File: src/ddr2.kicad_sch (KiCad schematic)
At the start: 7 parts, among them U2 IS43DR86400E

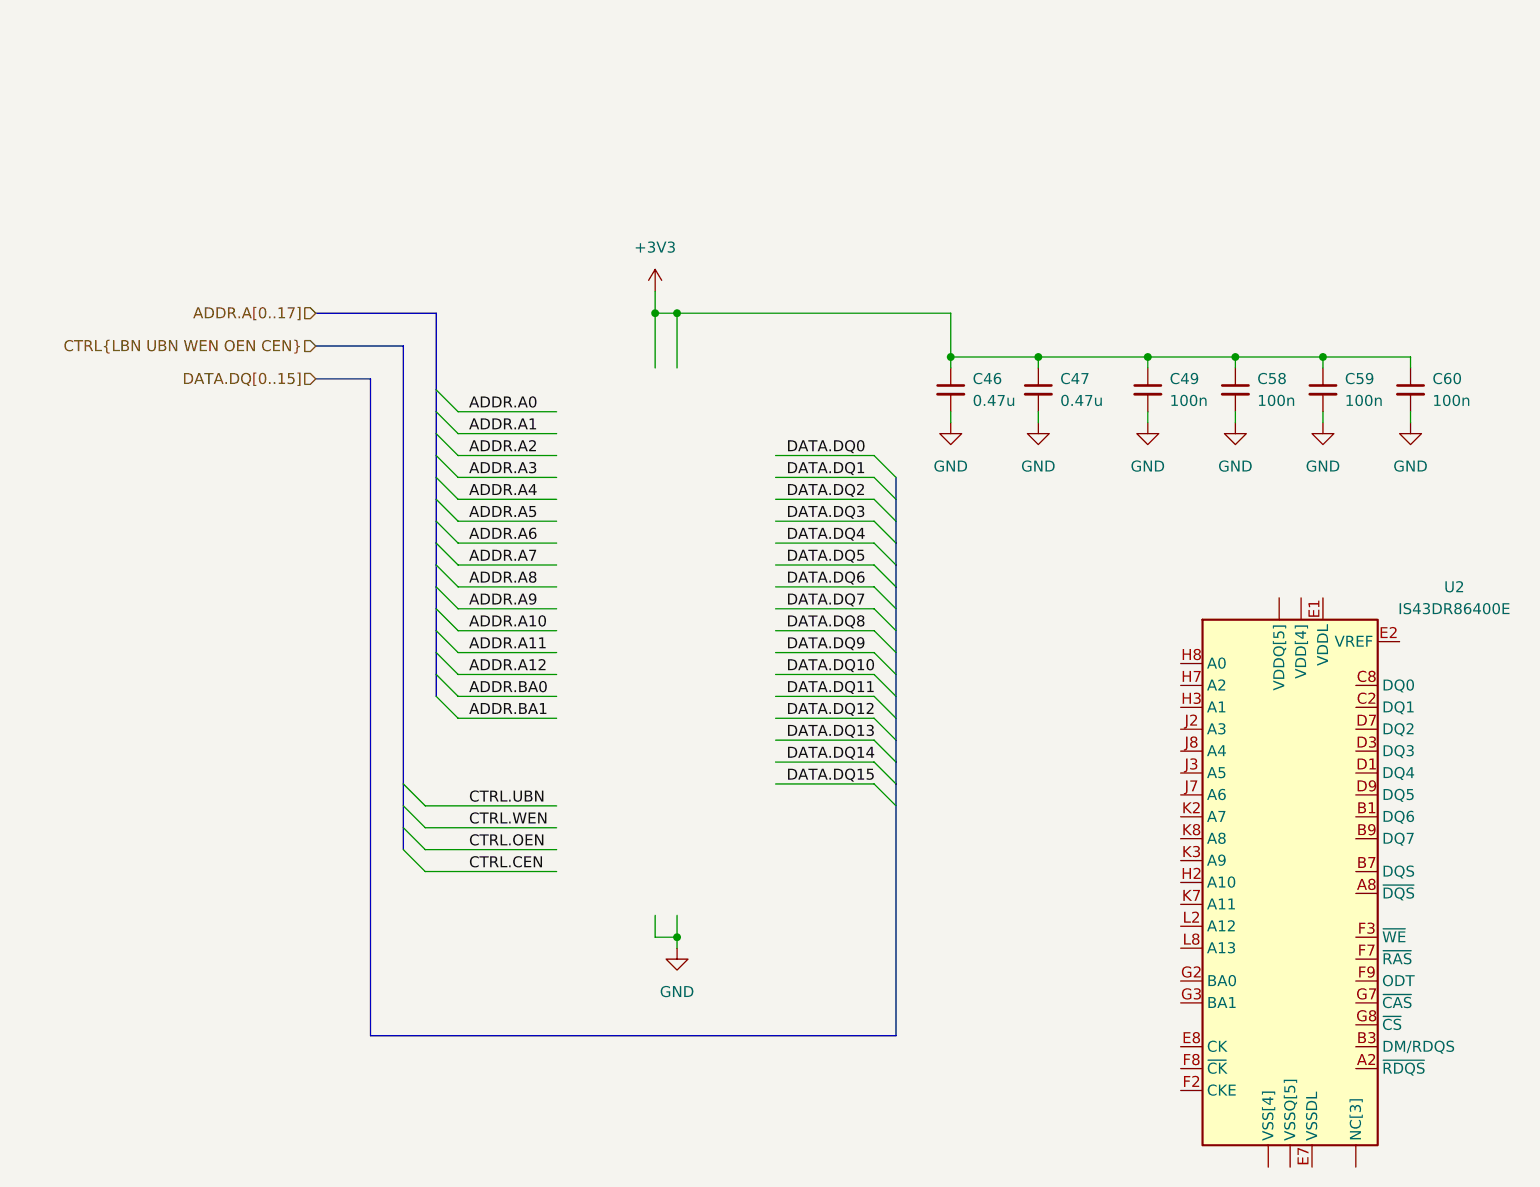
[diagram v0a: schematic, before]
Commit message: Adds DDR2 schematic
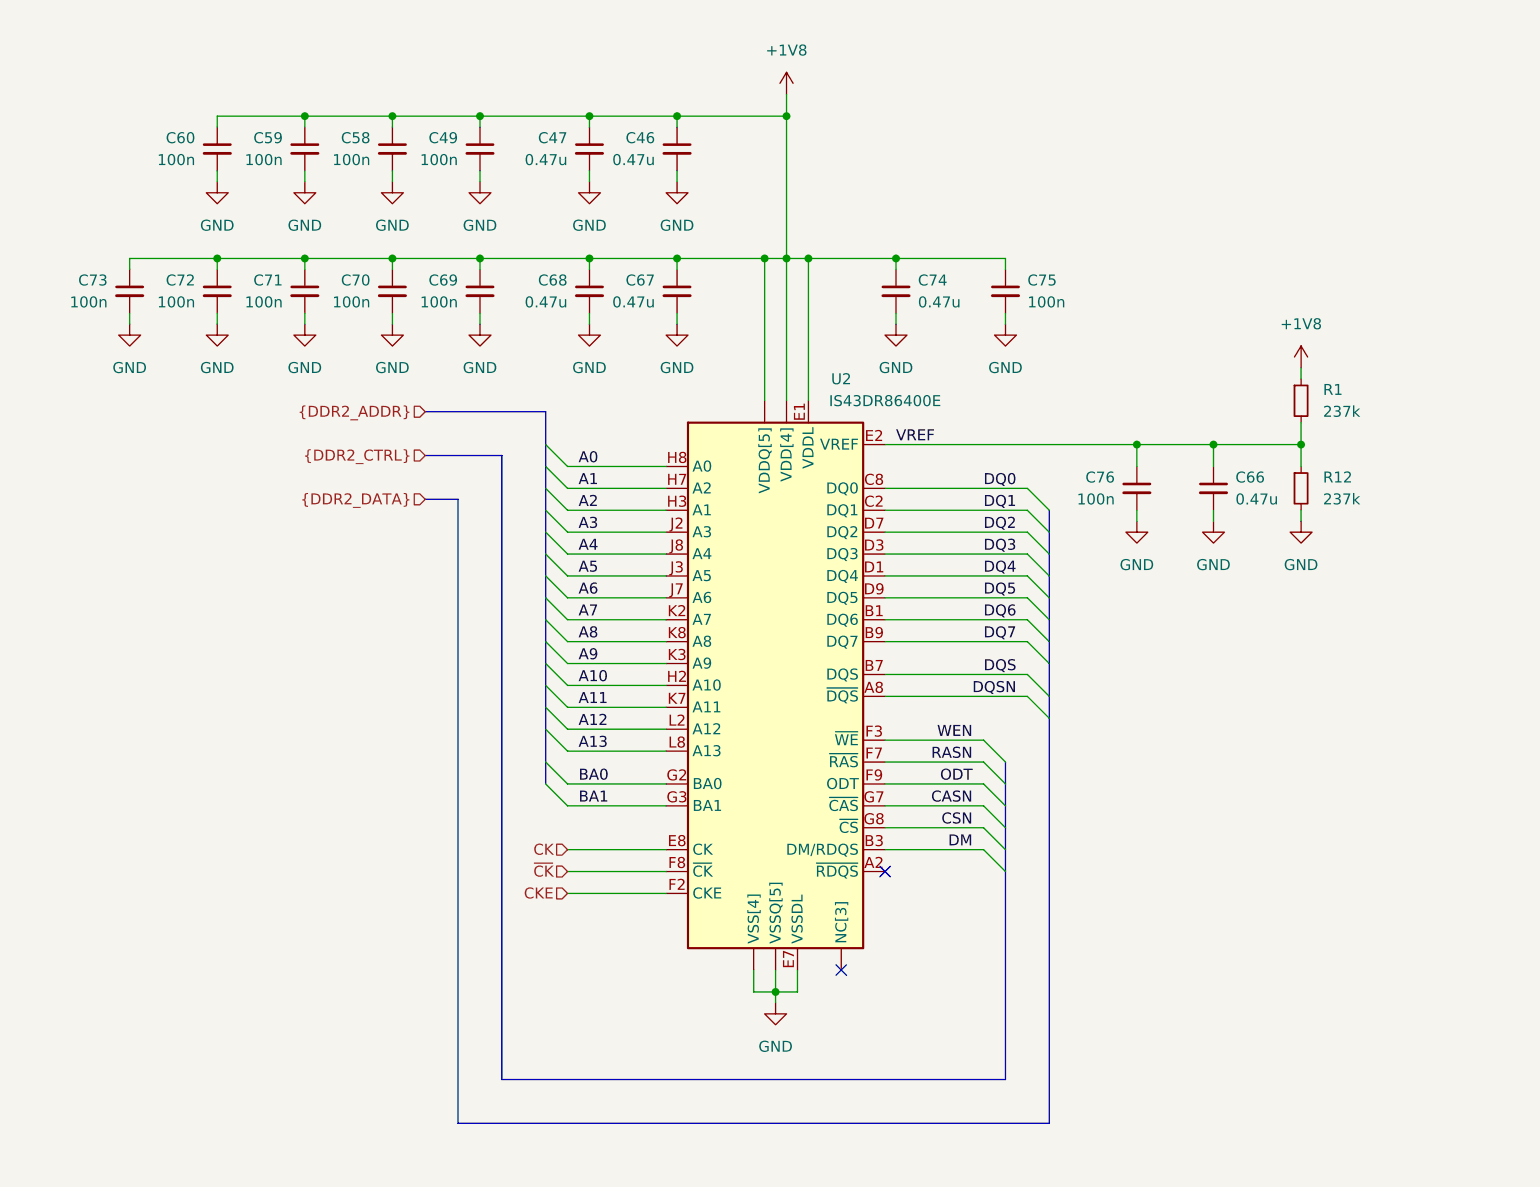
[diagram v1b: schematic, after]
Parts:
- added C66, C67, C68, C74: 0.47u, symbol Device:C_Small
- added C69, C70, C71, C72, C73, C75, C76: 100n, symbol Device:C_Small
- added R1, R12: 237k, symbol Device:R_Small
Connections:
- net +3V3 is gone; now on net +1V8: C46.1, C47.1, C49.1, C58.1, C59.1, C60.1
- net GND: now also U2. (VSS[4]), U2.A3 (VSS), U2.A7 (VSSQ), U2.B2 (VSSQ), U2.B8 (VSSQ), U2.D2 (VSSQ), U2.D8 (VSSQ), U2.E3 (VSS), U2.E7 (VSSDL), U2.J1 (VSS), U2.K9 (VSS), C66.2, C67.2, C68.2, C69.2, C70.2, C71.2, C72.2, C73.2, C74.2, C75.2, C76.2, R12.2
- net +1V8: now reaches U2. (VSS[4]), U2.A1 (VDD), U2.E9 (VDD), U2.H9 (VDD), U2.L1 (VDD)
- net +1V8: now also U2.A9 (VDDQ), U2.C1 (VDDQ), U2.C3 (VDDQ), U2.C7 (VDDQ), U2.C9 (VDDQ), U2.E1 (VDDL), C67.1, C68.1, C69.1, C70.1, C71.1, C72.1, C73.1, C74.1, C75.1, R1.1
- net DQSN: now reaches U2.A8 (~{DQS})
- net DQ6: now reaches U2.B1 (DQ6)
- net DM: now reaches U2.B3 (DM/RDQS)
- net DQS: now reaches U2.B7 (DQS)
- net DQ7: now reaches U2.B9 (DQ7)
- net DQ1: now reaches U2.C2 (DQ1)
- net DQ0: now reaches U2.C8 (DQ0)
- net DQ4: now reaches U2.D1 (DQ4)
- net DQ3: now reaches U2.D3 (DQ3)
- net DQ2: now reaches U2.D7 (DQ2)
- net DQ5: now reaches U2.D9 (DQ5)
- net VREF: now reaches U2.E2 (VREF)
- net VREF: now also C66.1, C76.1, R1.2, R12.1
- net CK: now reaches U2.E8 (CK)
- net CKE: now reaches U2.F2 (CKE)
- net WEN: now reaches U2.F3 (~{WE})
- net RASN: now reaches U2.F7 (~{RAS})
- net ~{CK}: now reaches U2.F8 (~{CK})
- net ODT: now reaches U2.F9 (ODT)
- net BA0: now reaches U2.G2 (BA0)
- net BA1: now reaches U2.G3 (BA1)
- net CASN: now reaches U2.G7 (~{CAS})
- net CSN: now reaches U2.G8 (~{CS})
- net A10: now reaches U2.H2 (A10)
- net A2: now reaches U2.H3 (A1)
- net A1: now reaches U2.H7 (A2)
- net A0: now reaches U2.H8 (A0)
- net A3: now reaches U2.J2 (A3)
- net A5: now reaches U2.J3 (A5)
- net A6: now reaches U2.J7 (A6)
- net A4: now reaches U2.J8 (A4)
- net A7: now reaches U2.K2 (A7)
- net A9: now reaches U2.K3 (A9)
- net A11: now reaches U2.K7 (A11)
- net A8: now reaches U2.K8 (A8)
- net A12: now reaches U2.L2 (A12)
- net A13: now reaches U2.L8 (A13)
- no-connect marks 0 -> 2
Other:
- moved on the sheet: U2

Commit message: Finishes the ram schematic
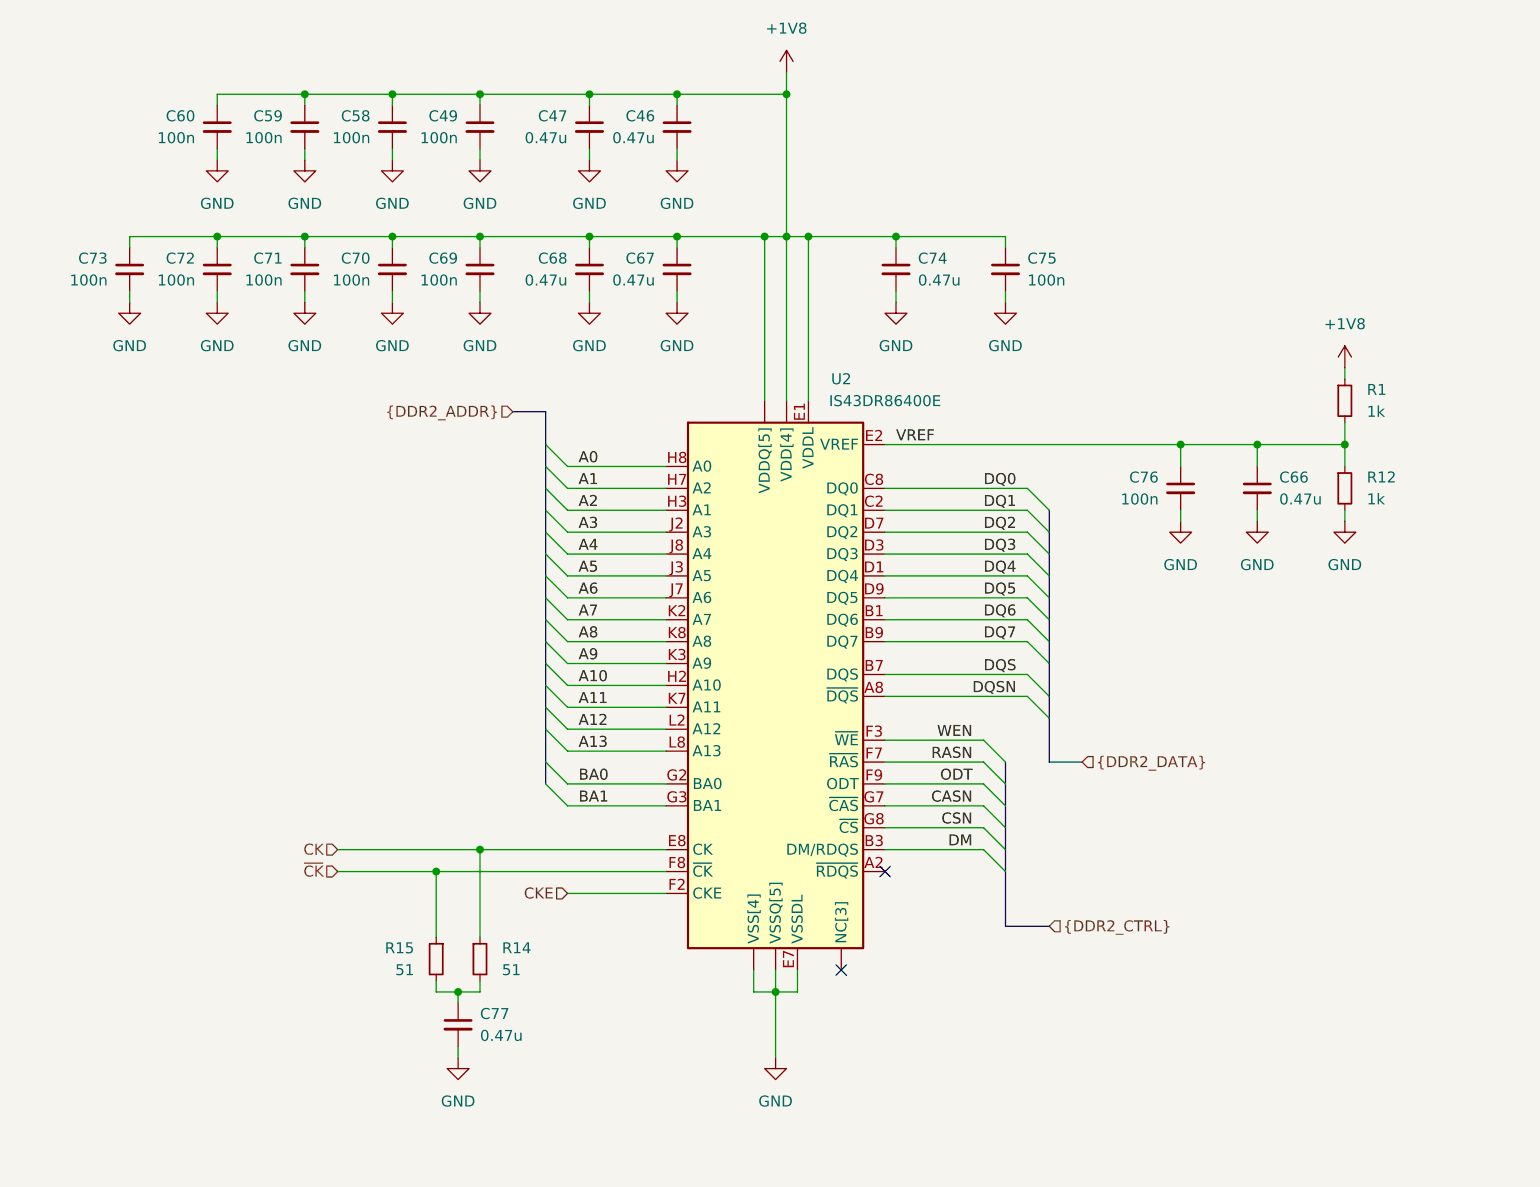
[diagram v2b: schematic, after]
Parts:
- added C77: 0.47u, symbol Device:C_Small
- added R14, R15: 51, symbol Device:R_Small
- R1, R12: value 237k -> 1k
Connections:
- net CK: now also R14.1
- net GND: now also C77.2
- net ~{CK}: now also R15.1
- new net: C77.1, R14.2, R15.2
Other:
- moved on the sheet: C46, C47, C49, C58, C59, C60, C66, C67, C68, C69, C70, C71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

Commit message: Add the eMMC
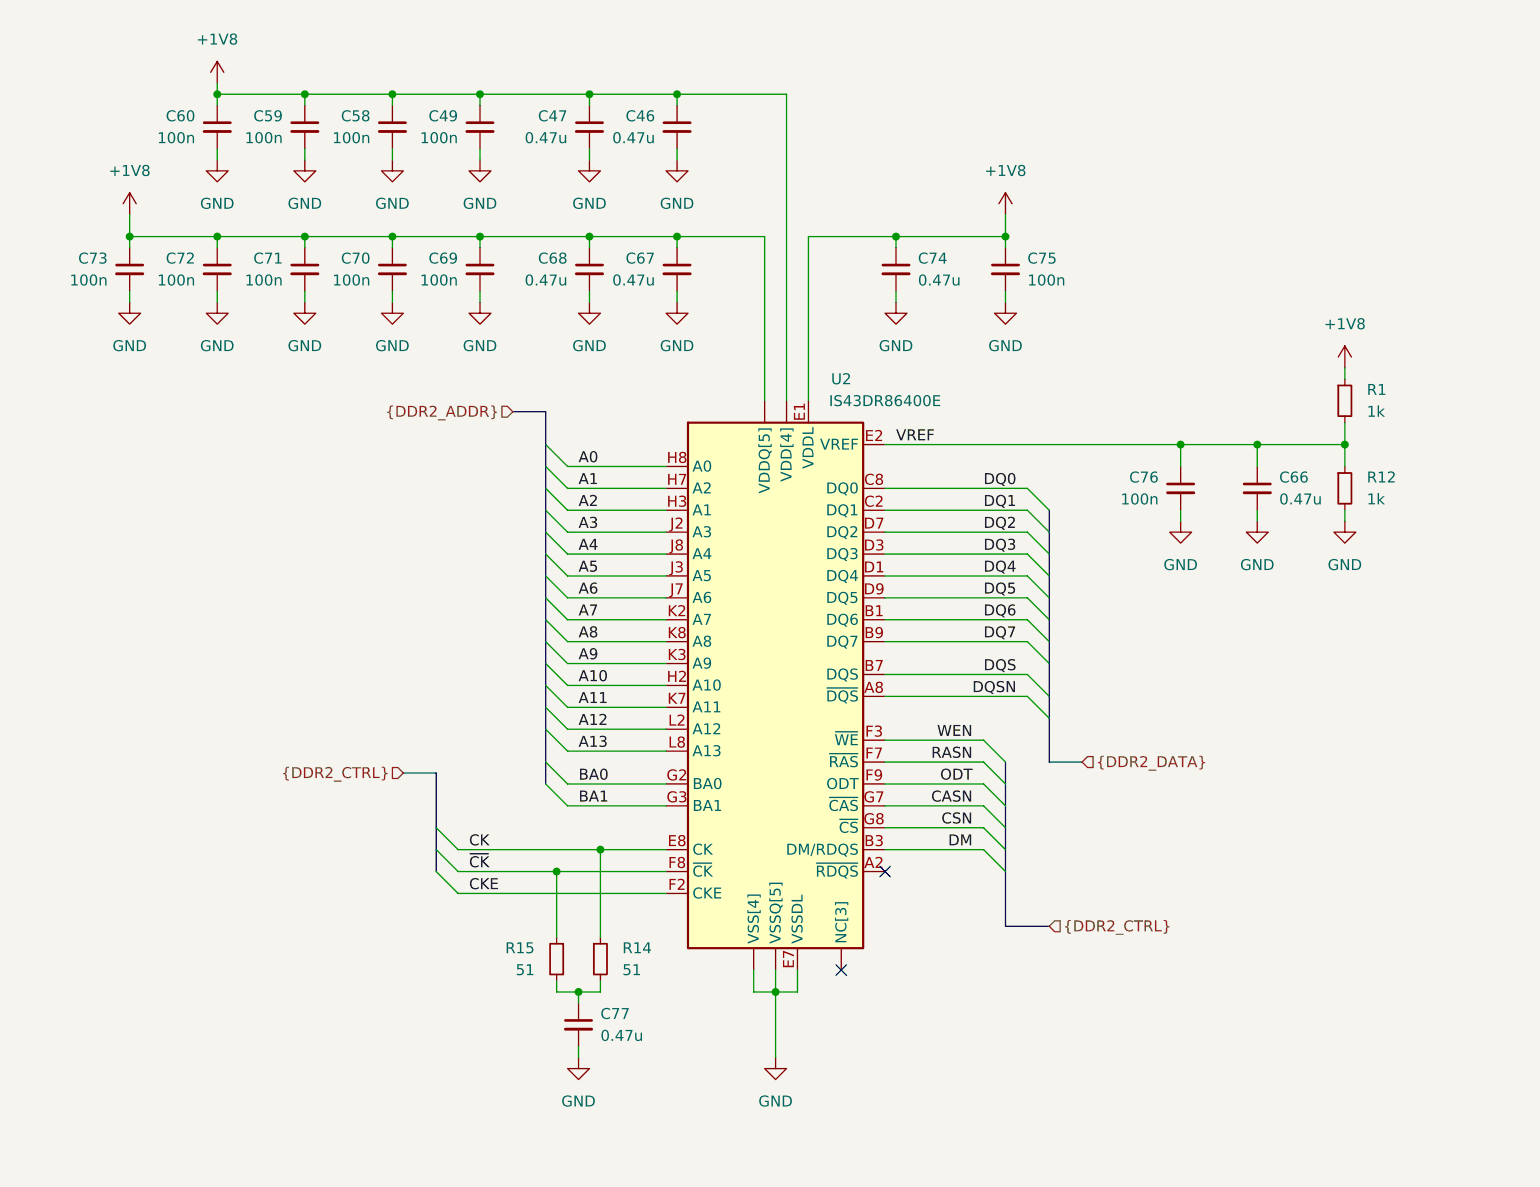
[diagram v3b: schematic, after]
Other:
- moved on the sheet: C77, R14, R15

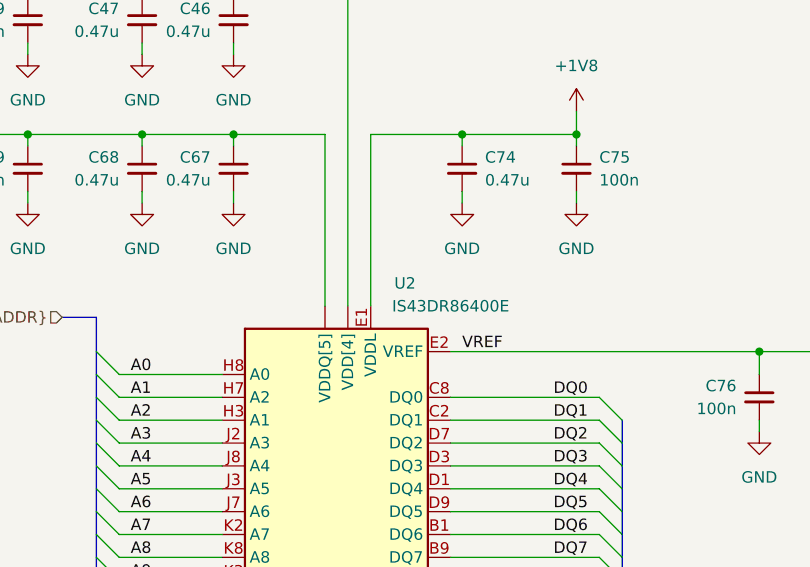
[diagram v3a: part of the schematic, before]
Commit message: Updates the structure of the schematic
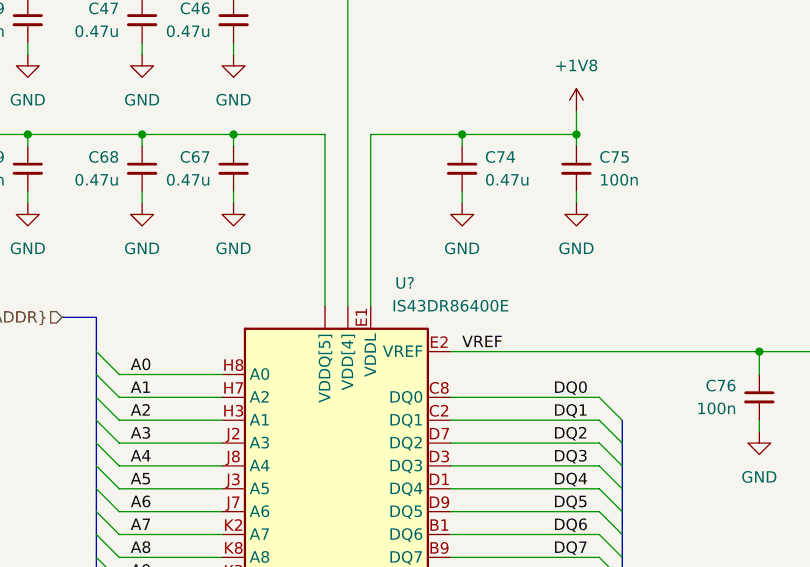
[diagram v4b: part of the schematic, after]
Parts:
- renumbered U2 to U?
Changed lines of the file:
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@@
 		(on_board yes)
 		(dnp no)
-		(property "Reference" "U2"
+		(property "Reference" "U?"
 			(at 157.48 64.8014 0)
 			(effects
@@
 		)
 		(instances
-			(project ""
+			(project "ecap5-bsom"
 				(path "/c5fd18a3-9aa0-4151-b6e0-94da3d606686/0481f44a-3ae5-4dda-99d2-682482abdf58"
-					(reference "U2")
+					(reference "U?")
 					(unit 1)
 				)
